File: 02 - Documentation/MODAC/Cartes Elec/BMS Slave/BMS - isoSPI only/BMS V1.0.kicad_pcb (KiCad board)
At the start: 2 copper layers, 144.5 x 54.5 mm, 108 parts, among them IC1 LT3990EMSE#TRPBF, IC2 LTC6255IS6#TRMPBF, IC3 ADG728BRUZ-REEL7, IC4 ADG728BRUZ-REEL7, IC6 LTC6811IG-1#PBF, J1 Conn_01x02_Pin, J2 Conn_01x07_Pin, J3 Conn_01x02_Pin, J4 Conn_01x08_Pin, J5 Conn_01x08_Pin, J6 Conn_01x07_Pin, Q1 Q_PMOS_GDS, Q10 Q_PMOS_GDS, Q11 Q_PMOS_GDS, Q12 Q_PMOS_GDS, Q2 Q_PMOS_GDS, Q3 Q_PMOS_GDS, Q4 Q_PMOS_GDS, Q5 Q_PMOS_GDS, Q6 Q_PMOS_GDS, Q7 Q_PMOS_GDS, Q8 Q_PMOS_GDS, Q9 Q_PMOS_GDS, T1 SM91501ALE

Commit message: Prise en compte retours JDL
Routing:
- net +5V: track 295.1 -> 201.9 mm, vias 5 -> 7
- net -VDC: track 33.6 -> 37.5 mm, vias 12 -> 22

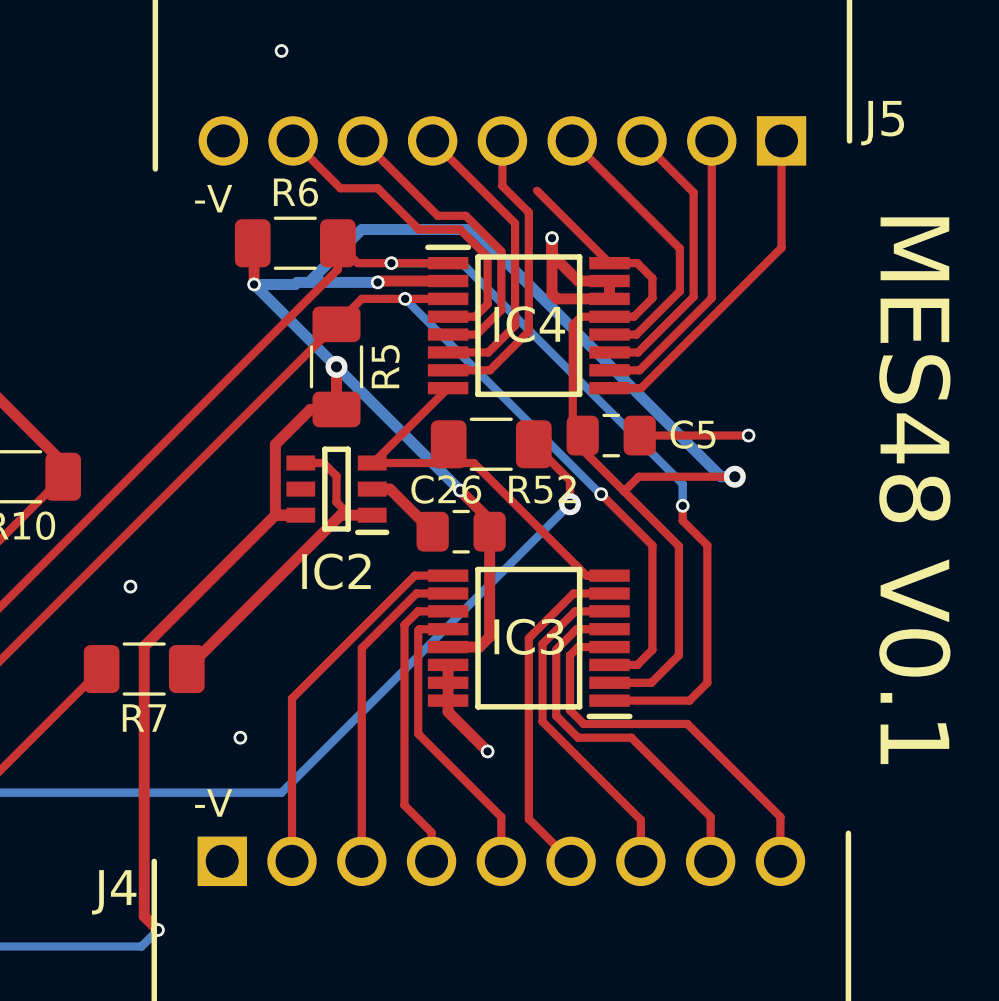
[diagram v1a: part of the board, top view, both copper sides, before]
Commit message: Modifs légères BMS/AMS
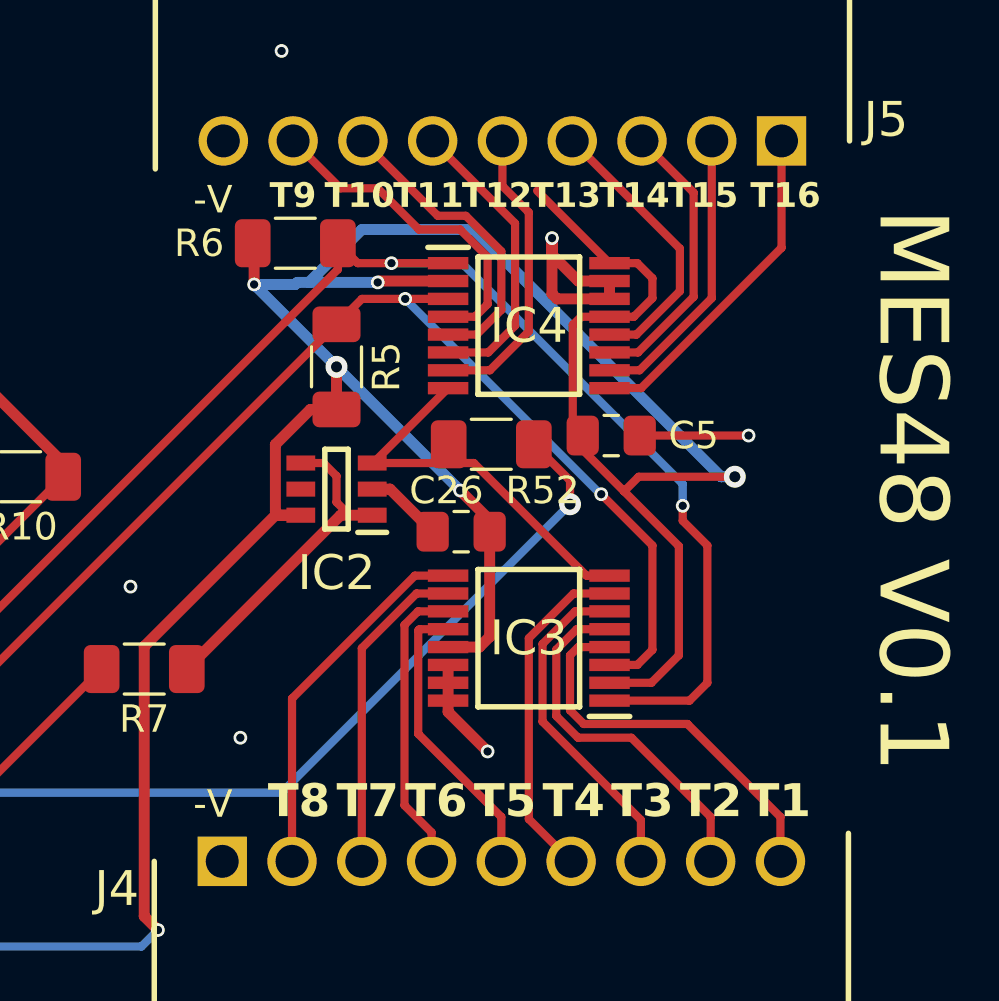
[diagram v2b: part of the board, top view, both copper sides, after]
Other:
- board text added: "T1"
- board text added: "T10"
- board text added: "T11"
- board text added: "T12"
- board text added: "T13"
- board text added: "T14"
- board text added: "T15"
- board text added: "T16"
- board text added: "T2"
- board text added: "T3"
- board text added: "T4"
- board text added: "T5"
- board text added: "T6"
- board text added: "T7"
- board text added: "T8"
- board text added: "T9"
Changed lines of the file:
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@@
 		(tags "resistor handsolder")
 		(property "Reference" "R6"
-			(at 0 -1.82 0)
+			(at -3.5 0 0)
 			(layer "F.SilkS")
 			(effects
@@
 		(layer "User.1")
 	)
+	(gr_text "T4"
+		(at 187.5 102.5 0)
+		(layer "F.SilkS")
+		(effects
+			(font
+				(size 1.2 1.2)
+				(thickness 0.2)
+				(bold yes)
+			)
+			(justify left bottom)
+		)
+	)
 	(gr_text "IM"
 		(at 165.5 65 0)
@@
 		)
 	)
+	(gr_text "T3"
+		(at 190 102.5 0)
+		(layer "F.SilkS")
+		(effects
+			(font
+				(size 1.2 1.2)
+				(thickness 0.2)
+				(bold yes)
+			)
+			(justify left bottom)
+		)
+	)
+	(gr_text "T13"
+		(at 187.063923 80.285286 0)
+		(layer "F.SilkS")
+		(effects
+			(font
+				(size 0.9 0.9)
+				(thickness 0.2)
+				(bold yes)
+			)
+			(justify left bottom)
+		)
+	)
 	(gr_text "10\n"
 		(at 86.5 102.5 0)
@@
 		)
 	)
+	(gr_text "T2"
+		(at 192.5 102.5 0)
+		(layer "F.SilkS")
+		(effects
+			(font
+				(size 1.2 1.2)
+				(thickness 0.2)
+				(bold yes)
+			)
+			(justify left bottom)
+		)
+	)
 	(gr_text "4"
 		(at 79 102.5 0)
@@
 		)
 	)
+	(gr_text "T1"
+		(at 195 102.5 0)
+		(layer "F.SilkS")
+		(effects
+			(font
+				(size 1.2 1.2)
+				(thickness 0.2)
+				(bold yes)
+			)
+			(justify left bottom)
+		)
+	)
 	(gr_text "Mandolule"
 		(at 136 116 0)
@@
 		)
 	)
+	(gr_text "T11"
+		(at 182.063923 80.285286 0)
+		(layer "F.SilkS")
+		(effects
+			(font
+				(size 0.9 0.9)
+				(thickness 0.2)
+				(bold yes)
+			)
+			(justify left bottom)
+		)
+	)
+	(gr_text "T10"
+		(at 179.563923 80.285286 0)
+		(layer "F.SilkS")
+		(effects
+			(font
+				(size 0.9 0.9)
+				(thickness 0.2)
+				(bold yes)
+			)
+			(justify left bottom)
+		)
+	)
 	(gr_text "IP"
 		(at 163 65 0)
@@
 		)
 	)
+	(gr_text "T9"
+		(at 177.563923 80.285286 0)
+		(layer "F.SilkS")
+		(effects
+			(font
+				(size 0.9 0.9)
+				(thickness 0.2)
+				(bold yes)
+			)
+			(justify left bottom)
+		)
+	)
 	(gr_text "5"
 		(at 84.5 80.5 0)
@@
 		)
 	)
+	(gr_text "T16"
+		(at 195.063923 80.285286 0)
+		(layer "F.SilkS")
+		(effects
+			(font
+				(size 0.9 0.9)
+				(thickness 0.2)
+				(bold yes)
+			)
+			(justify left bottom)
+		)
+	)
 	(gr_text "B"
 		(at 159 65.5 0)
@@
 		)
 	)
+	(gr_text "T7"
+		(at 180 102.5 0)
+		(layer "F.SilkS")
+		(effects
+			(font
+				(size 1.2 1.2)
+				(thickness 0.2)
+				(bold yes)
+			)
+			(justify left bottom)
+		)
+	)
 	(gr_text "11"
 		(at 77 80.5 0)
@@
 		)
 	)
+	(gr_text "T8"
+		(at 177.5 102.5 0)
+		(layer "F.SilkS")
+		(effects
+			(font
+				(size 1.2 1.2)
+				(thickness 0.2)
+				(bold yes)
+			)
+			(justify left bottom)
+		)
+	)
+	(gr_text "T12"
+		(at 184.563923 80.285286 0)
+		(layer "F.SilkS")
+		(effects
+			(font
+				(size 0.9 0.9)
+				(thickness 0.2)
+				(bold yes)
+			)
+			(justify left bottom)
+		)
+	)
+	(gr_text "T15"
+		(at 192.063923 80.285286 0)
+		(layer "F.SilkS")
+		(effects
+			(font
+				(size 0.9 0.9)
+				(thickness 0.2)
+				(bold yes)
+			)
+			(justify left bottom)
+		)
+	)
 	(gr_text "8"
 		(at 84 102.5 0)
@@
 		)
 	)
+	(gr_text "T14"
+		(at 189.563923 80.285286 0)
+		(layer "F.SilkS")
+		(effects
+			(font
+				(size 0.9 0.9)
+				(thickness 0.2)
+				(bold yes)
+			)
+			(justify left bottom)
+		)
+	)
 	(gr_text "+V\n"
 		(at 89 102.5 0)
@@
 		)
 	)
+	(gr_text "T5"
+		(at 185 102.5 0)
+		(layer "F.SilkS")
+		(effects
+			(font
+				(size 1.2 1.2)
+				(thickness 0.2)
+				(bold yes)
+			)
+			(justify left bottom)
+		)
+	)
 	(gr_text "A"
 		(at 168.5 65.5 0)
@@
 		)
 	)
+	(gr_text "T6"
+		(at 182.5 102.5 0)
+		(layer "F.SilkS")
+		(effects
+			(font
+				(size 1.2 1.2)
+				(thickness 0.2)
+				(bold yes)
+			)
+			(justify left bottom)
+		)
+	)

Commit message: Gerbers cartes modac
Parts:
- moved R50 1.50 mm to (155.5, 97.5)
- moved R49 1.12 mm to (150.5, 94.5), turned to 90 degrees
- moved R8 1.00 mm to (149.5, 90.0)
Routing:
- net Net-(IC6-ICMP): track 10.3 -> 14.2 mm
- net +5V: track 201.9 -> 198.1 mm
- net -VDC: track 37.5 -> 40.5 mm
- net Net-(IC6-IBIAS): track 3.50 -> 5.57 mm
- net /IMB: track 20.3 -> 21.5 mm
- net /IPB: track 13.6 -> 14.8 mm
- net Net-(C6-Pad2): track 4.90 -> 5.90 mm
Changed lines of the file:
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@@
 			(drillshape 0)
 			(scaleselection 1)
-			(outputdirectory "Export/")
+			(outputdirectory "../../../../BASTIE/Cartes Artemiz/Cirly/BMS/")
 		)
 	)
@@
 	(footprint "Resistor_SMD:R_1206_3216Metric_Pad1.30x1.75mm_HandSolder"
 		(layer "F.Cu")
-		(at 150 95.5)
+		(at 150.5 94.5 90)
 		(descr "Resistor SMD 1206 (3216 Metric), square (rectangular) end terminal, IPC_7351 nominal with elongated pad for handsoldering. (Body size source: IPC-SM-782 page 72, https://www.pcb-3d.com/wordpress/wp-content/uploads/ipc-sm-782a_amendment_1_and_2.pdf), generated with kicad-footprint-generator")
 		(tags "resistor handsolder")
 		(property "Reference" "R49"
-			(at -0.5 -1.96 0)
+			(at -0.5 -1.96 -90)
 			(layer "F.SilkS")
 			(effects
@@
 		)
 		(property "Value" "1k"
-			(at 0 1.82 0)
+			(at 0 1.82 -90)
 			(layer "F.Fab")
 			(effects
@@
 		)
 		(property "Footprint" "Resistor_SMD:R_1206_3216Metric_Pad1.30x1.75mm_HandSolder"
-			(at 0 0 0)
+			(at 0 0 90)
 			(unlocked yes)
 			(layer "F.Fab")
@@
 		)
 		(property "Datasheet" ""
-			(at 0 0 0)
+			(at 0 0 90)
 			(unlocked yes)
 			(layer "F.Fab")
@@
 		)
 		(property "Description" "Resistor"
-			(at 0 0 0)
+			(at 0 0 90)
 			(unlocked yes)
 			(layer "F.Fab")
@@
 		)
 		(fp_line
-			(start -2.45 -1.12)
-			(end 2.45 -1.12)
+			(start 2.45 -1.12)
+			(end 2.45 1.12)
 			(stroke
 				(width 0.05)
@@
 		)
 		(fp_line
-			(start -2.45 1.12)
-			(end -2.45 -1.12)
+			(start -2.45 -1.12)
+			(end 2.45 -1.12)
 			(stroke
 				(width 0.05)
@@
 		)
 		(fp_line
-			(start 2.45 -1.12)
-			(end 2.45 1.12)
+			(start 2.45 1.12)
+			(end -2.45 1.12)
 			(stroke
 				(width 0.05)
@@
 		)
 		(fp_line
-			(start 2.45 1.12)
-			(end -2.45 1.12)
+			(start -2.45 1.12)
+			(end -2.45 -1.12)
 			(stroke
 				(width 0.05)
@@
 		)
 		(fp_line
-			(start -1.6 -0.8)
-			(end 1.6 -0.8)
+			(start 1.6 -0.8)
+			(end 1.6 0.8)
 			(stroke
 				(width 0.1)
@@
 		)
 		(fp_line
-			(start -1.6 0.8)
-			(end -1.6 -0.8)
+			(start -1.6 -0.8)
+			(end 1.6 -0.8)
 			(stroke
 				(width 0.1)
@@
 		)
 		(fp_line
-			(start 1.6 -0.8)
-			(end 1.6 0.8)
+			(start 1.6 0.8)
+			(end -1.6 0.8)
 			(stroke
 				(width 0.1)
@@
 		)
 		(fp_line
-			(start 1.6 0.8)
-			(end -1.6 0.8)
+			(start -1.6 0.8)
+			(end -1.6 -0.8)
 			(stroke
 				(width 0.1)
@@
 		)
 		(fp_text user "${REFERENCE}"
-			(at 0 0 0)
+			(at 0 0 -90)
 			(layer "F.Fab")
 			(effects
@@
 		)
 		(pad "1" smd roundrect
-			(at -1.55 0)
+			(at -1.55 0 90)
 			(size 1.3 1.75)
 			(layers "F.Cu" "F.Paste" "F.Mask")
@@
 		)
 		(pad "2" smd roundrect
-			(at 1.55 0)
+			(at 1.55 0 90)
 			(size 1.3 1.75)
 			(layers "F.Cu" "F.Paste" "F.Mask")
@@
 	(footprint "Resistor_SMD:R_1206_3216Metric_Pad1.30x1.75mm_HandSolder"
 		(layer "F.Cu")
-		(at 150.5 90)
+		(at 149.5 90)
 		(descr "Resistor SMD 1206 (3216 Metric), square (rectangular) end terminal, IPC_7351 nominal with elongated pad for handsoldering. (Body size source: IPC-SM-782 page 72, https://www.pcb-3d.com/wordpress/wp-content/uploads/ipc-sm-782a_amendment_1_and_2.pdf), generated with kicad-footprint-generator")
 		(tags "resistor handsolder")
@@
 		(tags "SOT TO_SOT_SMD")
 		(property "Reference" "Q12"
-			(at 0 -2.4 180)
+			(at 4.05 -0.5 180)
 			(layer "F.SilkS")
 			(effects
@@
 	(footprint "Resistor_SMD:R_1206_3216Metric_Pad1.30x1.75mm_HandSolder"
 		(layer "F.Cu")
-		(at 154 97.55 -90)
+		(at 155.5 97.55 -90)
 		(descr "Resistor SMD 1206 (3216 Metric), square (rectangular) end terminal, IPC_7351 nominal with elongated pad for handsoldering. (Body size source: IPC-SM-782 page 72, https://www.pcb-3d.com/wordpress/wp-content/uploads/ipc-sm-782a_amendment_1_and_2.pdf), generated with kicad-footprint-generator")
 		(tags "resistor handsolder")
@@
 	)
 	(segment
-		(start 187.301282 79.588282)
-		(end 189.938 82.225)
-		(width 0.3)
-		(layer "F.Cu")
-		(net 2)
-	)
-	(segment
 		(start 192.4625 92.524451)
 		(end 192.4625 96.5)
@@
 	)
 	(segment
+		(start 153.5 94.075)
+		(end 156.4625 94.075)
+		(width 0.25)
+		(layer "F.Cu")
+		(net 6)
+	)
+	(segment
 		(start 187.844425 83.344425)
 		(end 187.844425 81.312811)
@@
 	)
 	(segment
+		(start 156.4625 94.075)
+		(end 156.5 94.0375)
+		(width 0.25)
+		(layer "F.Cu")
+		(net 6)
+	)
+	(segment
 		(start 181.3 90.45)
 		(end 181.95 90.45)
@@
 	)
 	(segment
-		(start 152.05 90)
+		(start 151.05 90)
 		(end 153.5 90)
 		(width 0.4)
@@
 	)
 	(segment
-		(start 148.2 95.75)
-		(end 148.45 95.5)
+		(start 148.5 96.05)
+		(end 150.5 96.05)
 		(width 0.3)
 		(layer "F.Cu")
@@
 	)
 	(segment
-		(start 151.55 95.5)
-		(end 153.5 95.5)
+		(start 148.2 95.75)
+		(end 148.5 96.05)
+		(width 0.3)
+		(layer "F.Cu")
+		(net 77)
+	)
+	(segment
+		(start 153.55 96)
+		(end 155.5 96)
 		(width 0.3)
 		(layer "F.Cu")
@@
 	)
 	(segment
-		(start 153.5 95.5)
-		(end 154 96)
+		(start 149.126472 92.95)
+		(end 150.5 92.95)
 		(width 0.3)
 		(layer "F.Cu")
@@
 	)
 	(segment
-		(start 148.076472 94)
-		(end 150.05 94)
+		(start 150.5 92.95)
+		(end 153.55 96)
 		(width 0.3)
 		(layer "F.Cu")
@@
 	)
 	(segment
-		(start 150.05 94)
-		(end 151.55 95.5)
+		(start 154 96)
+		(end 155.5 96)
 		(width 0.3)
 		(layer "F.Cu")
@@
 	(segment
 		(start 146.826472 95.25)
-		(end 148.076472 94)
+		(end 149.126472 92.95)
 		(width 0.3)
 		(layer "F.Cu")
@@
 	)
 	(segment
-		(start 157.565963 93.020065)
-		(end 158.05 92.536028)
+		(start 158.05 92.536028)
+		(end 158.05 90)
 		(width 0.3)
 		(layer "F.Cu")
@@
 	)
 	(segment
-		(start 158.05 92.536028)
-		(end 158.05 90)
+		(start 146.457106 94.75)
+		(end 149.707106 91.5)
 		(width 0.3)
 		(layer "F.Cu")
@@
 	)
 	(segment
-		(start 148.187041 93.020065)
-		(end 157.565963 93.020065)
+		(start 157.648528 92.9375)
+		(end 158.05 92.536028)
 		(width 0.3)
 		(layer "F.Cu")
@@
 	)
 	(segment
-		(start 146.457106 94.75)
-		(end 148.187041 93.020065)
+		(start 149.707106 91.5)
+		(end 151.332044 91.5)
 		(width 0.3)
 		(layer "F.Cu")
@@
 	)
 	(segment
+		(start 152.769544 92.9375)
+		(end 157.648528 92.9375)
+		(width 0.3)
+		(layer "F.Cu")
+		(net 79)
+	)
+	(segment
 		(start 158.5 86.345)
 		(end 158.5 89.55)
@@
 	)
 	(segment
-		(start 148.95 91.55)
-		(end 148.95 90)
+		(start 151.332044 91.5)
+		(end 152.769544 92.9375)
 		(width 0.3)
 		(layer "F.Cu")
-		(net 80)
+		(net 79)
 	)
 	(segment
 		(start 146.25 94.25)
-		(end 148.95 91.55)
+		(end 147.95 92.55)
 		(width 0.3)
 		(layer "F.Cu")
@@
 	)
 	(segment
-		(start 154.5 86.345)
-		(end 152.605 86.345)
-		(width 0.4)
+		(start 147.95 92.55)
+		(end 147.95 90)
+		(width 0.3)
 		(layer "F.Cu")
 		(net 80)
 	)
 	(segment
-		(start 152.605 86.345)
-		(end 148.95 90)
+		(start 150.655 86.345)
+		(end 147.95 89.05)
 		(width 0.4)
 		(layer "F.Cu")
@@
 		(layer "F.Cu")
 		(net 80)
+	)
+	(segment
+		(start 154.5 86.345)
+		(end 150.655 86.345)
+		(width 0.4)
+		(layer "F.Cu")
+		(net 80)
+	)
+	(segment
+		(start 147.95 89.05)
+		(end 147.95 90)
+		(width 0.4)
+		(layer "F.Cu")
+		(net 80)

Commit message: MAJ AMS/BMS
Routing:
- net /Cell 1: track 56.7 -> 57.8 mm
- net /SCL: track 74.7 -> 75.5 mm
- net +5V: track 198.1 -> 197.5 mm
- net /SDA: track 66.1 -> 66.6 mm
